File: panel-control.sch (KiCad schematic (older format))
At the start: 48 parts, among them J1 40HAT, J2 Conn_01x04, J3 103904-3, J4 HUB-75, J5 PWR, Q1 DMG2305UX, Q2 AO4407A, Q3 DMMT5401, SW1 RST, U1 STM8S003F3P, U2 TXS0108EPW, U3 TXS0108EPW

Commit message: fix labels and tweak pwr_en
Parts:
- removed J3: 103904-3, user_footprints:TE_103904-3, symbol 103904-3:103904-3
- added J4: HUB-75_B, user_footprints:TE_5-103167-5, symbol Connector_Generic:Conn_02x08_Odd_Even
- added J6: Conn_01x02_Male, symbol Connector:Conn_01x02_Male
- added R5: 5k, Resistor_SMD:R_0603_1608Metric, symbol Device:R
- added R7: 5k, symbol Device:R
- added U3: TXS0108EPW, Package_SO:TSSOP-20_4.4x6.5mm_P0.65mm, symbol Logic_LevelTranslator:TXS0108EPW
- C3: renamed from C6; value 1uF -> 100nF
- C4: renamed from C7; value 1uF -> 100nF
- J1: renamed from J5; footprint Connector_PinHeader_2.54mm:PinHeader_2x02_P2.54mm_Vertical -> Connector_PinHeader_2.54mm:PinHeader_2x04_P2.54mm_Vertical; symbol Connector_Generic:Conn_02x02_Odd_Even -> Connector_Generic:Conn_02x04_Odd_Even
- J3: renamed from J4; value HUB-75 -> HUB-75_A
- J5: renamed from J2; value Conn_01x04 -> SWIM
- MK1, MK2: symbol ICS-43434_DIP-6:ICS-43434 -> panel-control-rescue:ICS-43434-ICS-43434_DIP-6
- Q3: renamed from Q2; symbol AO4407A:AO4407A -> panel-control-rescue:AO4407A-AO4407A
- R6: renamed from R?; value 10k -> 1k
- gave numbers to parts that had none: 16
- renumbered C8 to C1, C2 to C10, C3 to C11, C4 to C12, C5 to C13, C9 to C2, C1 to C6, H3 to H2, H2 to H3, J1 to J2, Q3 to Q1, Q1 to Q2, R4 to R1, R1 to R2, R2 to R3, R3 to R4, SW1 to SW2, U3 to U1, U1 to U5
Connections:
- net labels added: B1A_A, B1A_B, B1B_A, B1B_B, B2A_A, B2A_B, B2B_A, B2B_B, G1A_A, G1A_B, G1B_A, G1B_B, G2A_A, G2A_B, G2B_A, G2B_B, I2S_OUT, R1A_A, R1A_B, R1B_A, R1B_B, R2A_A, R2A_B, R2B_A, R2B_B
- net labels removed: B1_A, B1_B, B2_A, B2_B, G1_A, G1_B, G2_A, G2_B, R1_A, R1_B, R2_A, R2_B, SCL_A, SCL_B, SDA_A, SDA_B, VBUS
- wire segments 199 -> 246
- no-connect marks 0 -> 3
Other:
- note added: "LED Panel Connectors"
- note removed: "LED Strip Connector"
- note removed: "SWIM"
- moved on the sheet: C10, C11, C12, C13, C6, J3, J5, R9, SW2

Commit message: mainly finished schematic revision
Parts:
- removed C6: 100nF, Capacitor_SMD:C_0603_1608Metric, symbol Device:C
- added C11: 100nF, Capacitor_SMD:C_0603_1608Metric, symbol Device:C
- added C12, C15: 100nF, Capacitor_SMD:C_0603_1608Metric_Pad1.08x0.95mm_HandSolder, symbol Device:C
- added D1: 5V, LED_SMD:LED_0603_1608Metric, symbol Device:LED
- added D3: PI, LED_SMD:LED_0603_1608Metric, symbol Device:LED
- added J6: POWER_CONN, symbol Connector:Conn_01x06_Male
- added R12: 4.7k, Resistor_SMD:R_0603_1608Metric, symbol Device:R
- added R14, R16: 470, Resistor_SMD:R_0603_1608Metric, symbol Device:R
- J2: renamed from J6; value Conn_01x02_Male -> VBAT
- R3: renamed from R5; value 5k -> 4.7k
- R5: renamed from R6; value 1k -> 4.7k
- R7: value 5k -> 10k
- SW1: value RST -> POW
- SW2: value RST -> NRST
- renumbered C7 to C1, C5 to C10, C1 to C13, C2 to C14, C9 to C2, C10 to C3, C11 to C4, C12 to C5, C13 to C6, C8 to C7, C3 to C8, C4 to C9, D1 to D2, D2 to D4, H3 to H2, H2 to H3, J2 to J1, J1 to J5, J5 to J7, Q3 to Q1, Q4 to Q2, Q2 to Q3, Q1 to Q4, R9 to R1, R4 to R10, R8 to R11, R1 to R13, R11 to R15, R12 to R17, R10 to R2, R13 to R4, R14 to R6, R3 to R8, R2 to R9, U4 to U1, U5 to U2, U2 to U3, U1 to U4, U3 to U5
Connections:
- net +3.3VA: now also C15.1
- net +3V3: now also J6.1 (Pin_1), R12.1
- net +5VA: now also Q1.1, Q1.2, Q1.3, R3.2, C12.1, R14.1; no longer Q3.3 (D), Q4.6 (E)
- net GND: now also C11.1, C12.2, C15.2, D1.1 (K), J6.6 (Pin_6); no longer D4.1 (K)
- net LED_BAT: now also J6.5 (Pin_5)
- net LED_PWR: now also J6.4 (Pin_4)
- net P5V_HAT: now also Q3.2 (S), Q4.6 (E), R16.1; no longer Q1.5, Q1.6, Q1.7, Q1.8
- net at Q3.1 (G), R8.1: now also Q4.1 (C); no longer Q4.4 (C)
- net NRST: now reaches SW2.1, U2.4 (NRST)
- net NRST: now also C11.2, J6.3 (Pin_3), R12.2; no longer J7.4 (Pin_4)
- net POW renamed BUT_POW
- new net: Q4.2 (B), Q4.3 (B), Q4.4 (C), R9.1
- new net: D3.1 (K), D4.1 (K)
- new net: D1.2 (A), R14.2
- new net: D3.2 (A), R16.2
- new net BUT_PWR: J6.2 (Pin_2)
- new net EXT_5V: Q1.5, Q1.6, Q1.7, Q1.8, Q3.3 (D), Q4.5 (E)
- new net RST: J7.4 (Pin_4)
- no-connect marks 3 -> 11
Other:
- note added: "I think this is intended to block excessive current\nfrom flowing from the Pi to the Hat, but actually idk.."
- note removed: "This is based on the official Raspberry Pi spec to be able to call an extension board a HAT.\nhttps://github.com/raspberrypi/hats/blob/master/designguide.md"
- moved on the sheet: C1, C10, C13, C14, C2, C3, C4, C5, C6, C7, D2, D4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

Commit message: update pcb from new sch
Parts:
- C3, C4, C5, C6: footprint (none) -> Capacitor_SMD:C_0603_1608Metric
- C7, R7: footprint (none) -> Resistor_SMD:R_0603_1608Metric
- J2: footprint (none) -> Connector_PinHeader_2.54mm:PinHeader_1x02_P2.54mm_Vertical
- J6: footprint (none) -> Connector_PinHeader_2.54mm:PinHeader_1x06_P2.54mm_Vertical
- J7: footprint (none) -> Connector_PinHeader_2.54mm:PinHeader_1x04_P2.54mm_Vertical
- Q2: footprint Package_TO_SOT_THT:TO-92_Inline -> Package_TO_SOT_SMD:SOT-23
- U1: value AMS1117-3.3 -> HT7533-1; footprint Package_TO_SOT_SMD:SOT-223-3_TabPin2 -> Package_TO_SOT_SMD:SOT-89-3; symbol Regulator_Linear:AMS1117-3.3 -> Regulator_Linear:HT75xx-1-SOT89; LCSC C6186 -> C14289
- U2: value STM8S003F3P -> STM8S103F3P
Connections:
- net +3V3: now also U1.3 (VOUT); no longer U1.2 (VO)
- net +5VA: now also U1.2 (VIN); no longer U1.3 (VI)
- no-connect marks 11 -> 19
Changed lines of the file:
@@
 P 13000 3300
 F 0 "U2" H 13000 4481 50  0000 C CNN
-F 1 "STM8S003F3P" H 13000 4390 50  0000 C CNN
+F 1 "STM8S103F3P" H 13000 4390 50  0000 C CNN
 F 2 "Package_SO:TSSOP-20_4.4x6.5mm_P0.65mm" H 13050 4400 50  0001 L CNN
 F 3 "http://www.st.com/st-web-ui/static/active/en/resource/technical/document/datasheet/DM00024550.pdf" H 12950 2900 50  0001 C CNN
@@
 F 0 "J7" H 1068 9967 50  0000 C CNN
 F 1 "SWIM" H 1068 9876 50  0000 C CNN
-F 2 "" H 1150 9650 50  0001 C CNN
+F 2 "Connector_PinHeader_2.54mm:PinHeader_1x04_P2.54mm_Vertical" H 1150 9650 50  0001 C CNN
 F 3 "~" H 1150 9650 50  0001 C CNN
 	1    1150 9650
@@
 F 0 "C3" H 13486 1604 50  0000 R CNN
 F 1 "100nF" H 13486 1695 50  0000 R CNN
-F 2 "" H 13638 1500 50  0001 C CNN
+F 2 "Capacitor_SMD:C_0603_1608Metric" H 13638 1500 50  0001 C CNN
 F 3 "~" H 13600 1650 50  0001 C CNN
 	1    13600 1650
@@
 F 0 "C4" H 13736 1604 50  0000 R CNN
 F 1 "100nF" H 13736 1695 50  0000 R CNN
-F 2 "" H 13888 1500 50  0001 C CNN
+F 2 "Capacitor_SMD:C_0603_1608Metric" H 13888 1500 50  0001 C CNN
 F 3 "~" H 13850 1650 50  0001 C CNN
 	1    13850 1650
@@
 F 0 "C7" H 12085 4104 50  0000 R CNN
 F 1 "1uF" H 12085 4195 50  0000 R CNN
-F 2 "" H 12238 4000 50  0001 C CNN
+F 2 "Resistor_SMD:R_0603_1608Metric" H 12238 4000 50  0001 C CNN
 F 3 "~" H 12200 4150 50  0001 C CNN
 	1    12200 4150
@@
 F 3 "" H 14450 3400 50  0000 C CNN
 	1    14450 3400
-	1    0    0    -1
-$EndComp
-$Comp
-L Regulator_Linear:AMS1117-3.3 U1
-U 1 1 601B9BE5
-P 12500 1500
-F 0 "U1" H 12500 1742 50  0000 C CNN
-F 1 "AMS1117-3.3" H 12500 1651 50  0000 C CNN
-F 2 "Package_TO_SOT_SMD:SOT-223-3_TabPin2" H 12500 1700 50  0001 C CNN
-F 3 "http://www.advanced-monolithic.com/pdf/ds1117.pdf" H 12600 1250 50  0001 C CNN
-F 4 "C6186" H 12500 1500 50  0001 C CNN "LCSC"
-	1    12500 1500
 	1    0    0    -1
 $EndComp
@@
 F 0 "Q2" H 9341 2096 50  0000 L CNN
 F 1 "S8050" H 9341 2005 50  0000 L CNN
-F 2 "Package_TO_SOT_THT:TO-92_Inline" H 9350 1975 50  0001 L CIN
+F 2 "Package_TO_SOT_SMD:SOT-23" H 9350 1975 50  0001 L CIN
 F 3 "http://www.unisonic.com.tw/datasheet/S8050.pdf" H 9150 2050 50  0001 L CNN
 	1    9150 2050
@@
 F 0 "J2" H 15072 3024 50  0000 R CNN
 F 1 "VBAT" H 15072 2933 50  0000 R CNN
-F 2 "" H 15100 3050 50  0001 C CNN
+F 2 "Connector_PinHeader_2.54mm:PinHeader_1x02_P2.54mm_Vertical" H 15100 3050 50  0001 C CNN
 F 3 "~" H 15100 3050 50  0001 C CNN
 	1    15100 3050
@@
 F 0 "R7" H 9770 2246 50  0000 L CNN
 F 1 "10k" H 9770 2155 50  0000 L CNN
-F 2 "" V 9630 2200 50  0001 C CNN
+F 2 "Resistor_SMD:R_0603_1608Metric" V 9630 2200 50  0001 C CNN
 F 3 "~" H 9700 2200 50  0001 C CNN
 	1    9700 2200
@@
 F 0 "C6" H 14236 1604 50  0000 R CNN
 F 1 "100nF" H 14236 1695 50  0000 R CNN
-F 2 "" H 14388 1500 50  0001 C CNN
+F 2 "Capacitor_SMD:C_0603_1608Metric" H 14388 1500 50  0001 C CNN
 F 3 "~" H 14350 1650 50  0001 C CNN
 	1    14350 1650
@@
 F 0 "C5" H 13986 1604 50  0000 R CNN
 F 1 "100nF" H 13986 1695 50  0000 R CNN
-F 2 "" H 14138 1500 50  0001 C CNN
+F 2 "Capacitor_SMD:C_0603_1608Metric" H 14138 1500 50  0001 C CNN
 F 3 "~" H 14100 1650 50  0001 C CNN
 	1    14100 1650
@@
 F 0 "J6" H 1258 8431 50  0000 C CNN
 F 1 "POWER_CONN" H 1258 8340 50  0000 C CNN
-F 2 "" H 1150 8050 50  0001 C CNN
+F 2 "Connector_PinHeader_2.54mm:PinHeader_1x06_P2.54mm_Vertical" H 1150 8050 50  0001 C CNN
 F 3 "~" H 1150 8050 50  0001 C CNN
 	1    1150 8050
@@
 Text Label 7650 2150 0    50   ~ 0
 EXT_5V
+NoConn ~ 12400 3400
+NoConn ~ 12400 2800
+NoConn ~ 12400 2700
+NoConn ~ 12400 3500
+NoConn ~ 12400 3600
+NoConn ~ 12400 3700
+NoConn ~ 13600 3200
+NoConn ~ 13600 3300
+$Comp
+L Regulator_Linear:HT75xx-1-SOT89 U1
+U 1 1 601B9BE5
+P 12500 1600
+F 0 "U1" H 12500 1842 50  0000 C CNN
+F 1 "HT7533-1" H 12500 1751 50  0000 C CNN
+F 2 "Package_TO_SOT_SMD:SOT-89-3" H 12500 1800 50  0001 C CNN
+F 3 "https://www.holtek.com/documents/10179/116711/HT75xx-1v250.pdf" H 12600 1350 50  0001 C CNN
+F 4 "C14289" H 12500 1600 50  0001 C CNN "LCSC"
+	1    12500 1600
+	1    0    0    -1
+$EndComp
 $EndSCHEMATC

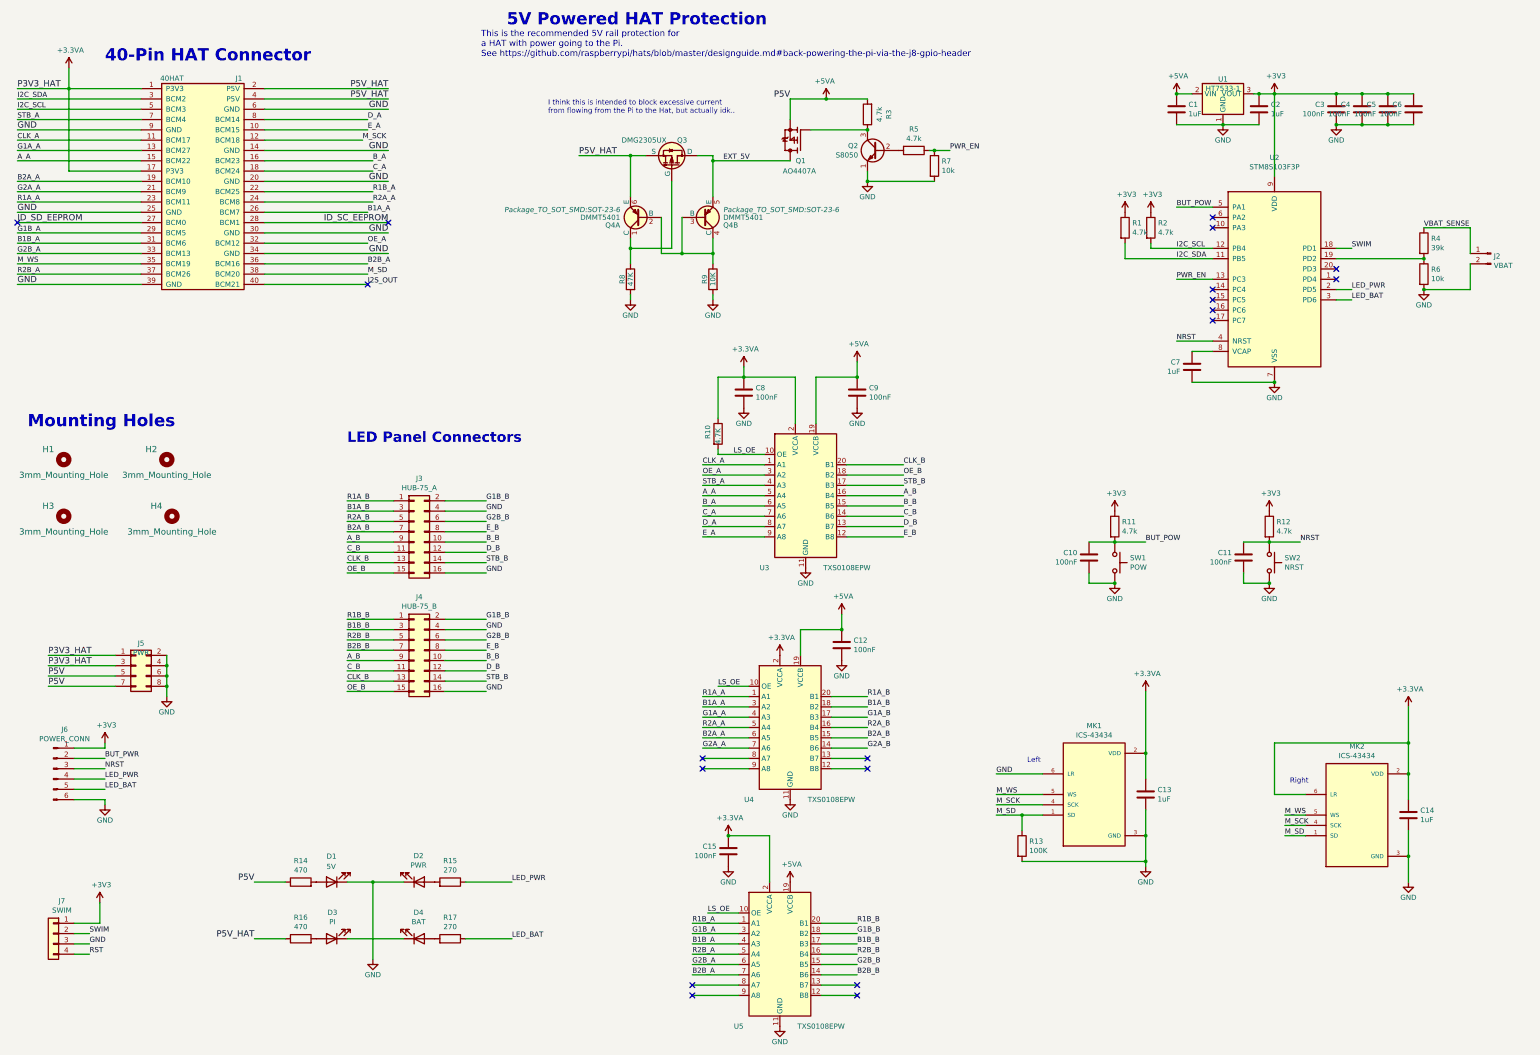
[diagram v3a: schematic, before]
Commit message: add fan connector to sch
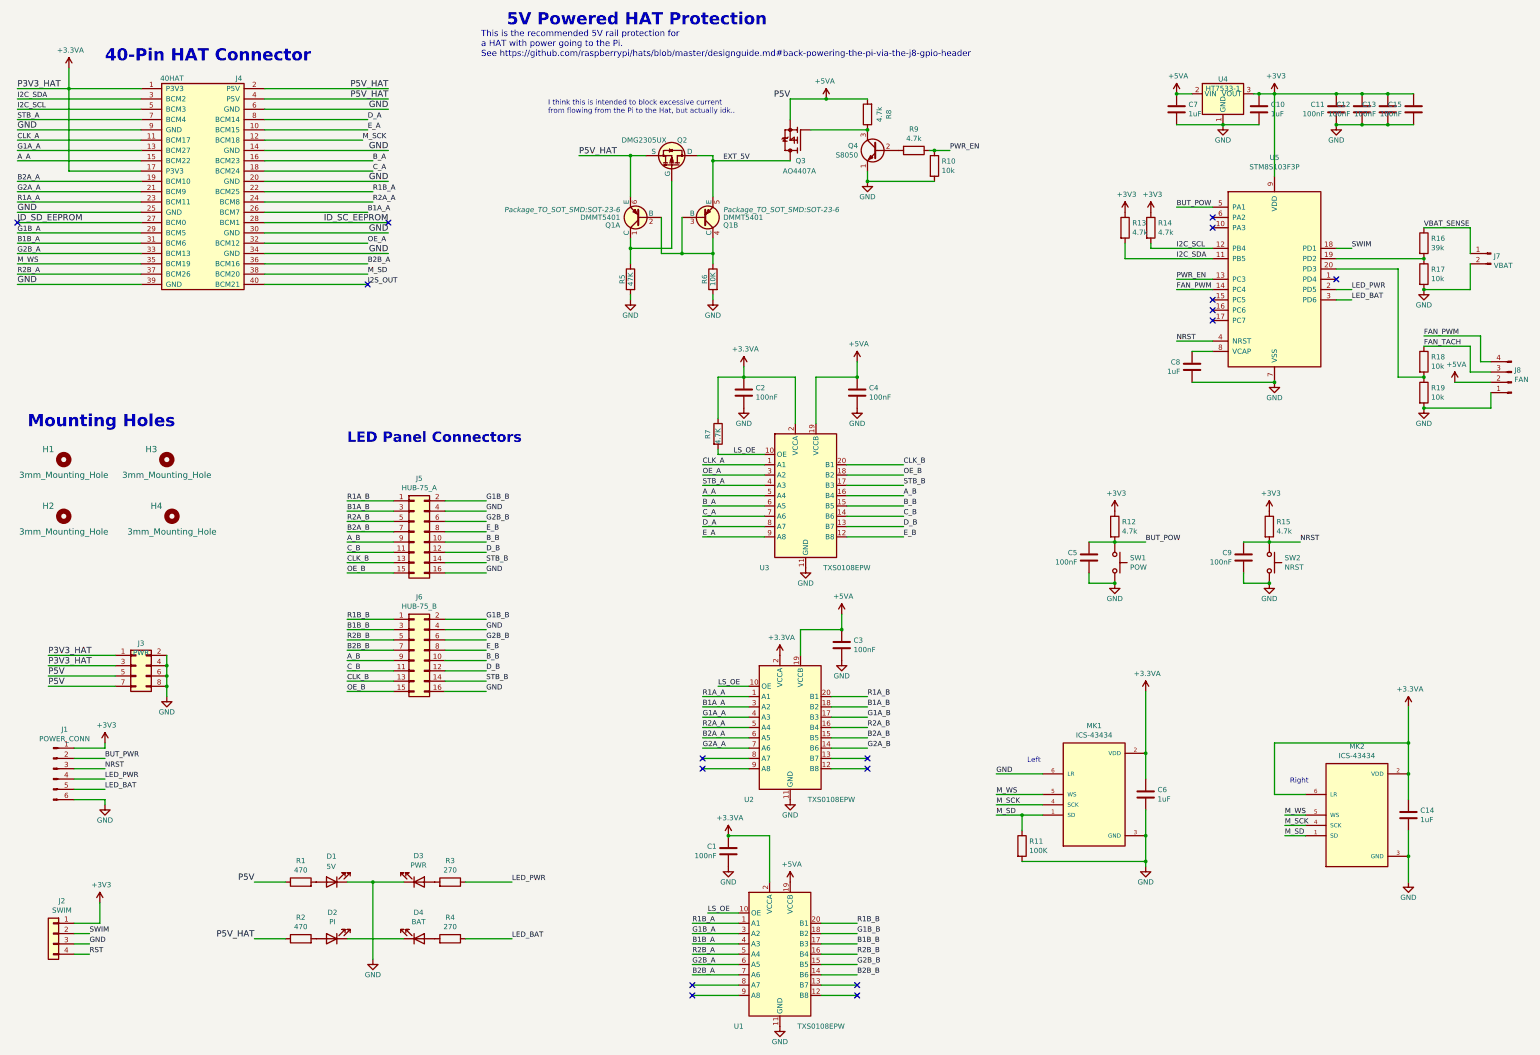
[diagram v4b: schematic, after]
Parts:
- added J8: FAN, Connector_PinSocket_2.54mm:PinSocket_1x04_P2.54mm_Vertical, symbol Connector:Conn_01x04_Male
- added R18, R19: 10k, Resistor_SMD:R_0603_1608Metric, symbol Device:R
- renumbered C15 to C1, C2 to C10, C3 to C11, C4 to C12, C5 to C13, C6 to C15, C8 to C2, C12 to C3, C9 to C4, C10 to C5, C13 to C6, C1 to C7, C7 to C8, C11 to C9, D3 to D2, D2 to D3, H3 to H2, H2 to H3, J6 to J1, J7 to J2, J5 to J3, J1 to J4, J3 to J5, J4 to J6, J2 to J7, Q4 to Q1, Q3 to Q2, Q1 to Q3, Q2 to Q4, R14 to R1, R7 to R10, R13 to R11, R11 to R12, R1 to R13, R2 to R14, R12 to R15, R4 to R16, R6 to R17, R16 to R2, R15 to R3, R17 to R4, R8 to R5, R9 to R6, R10 to R7, R3 to R8, R5 to R9, U5 to U1, U4 to U2, U1 to U4, U2 to U5
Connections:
- net +5VA: now also J8.2 (Pin_2)
- net GND: now also J8.1 (Pin_1), R19.2
- net FAN_PWM: now reaches U5.14 (PC4)
- net FAN_PWM: now also J8.4 (Pin_4)
- net at U5.20 (PD3): now also R18.2, R19.1
- new net FAN_TACH: J8.3 (Pin_3), R18.1
- no-connect marks 19 -> 17

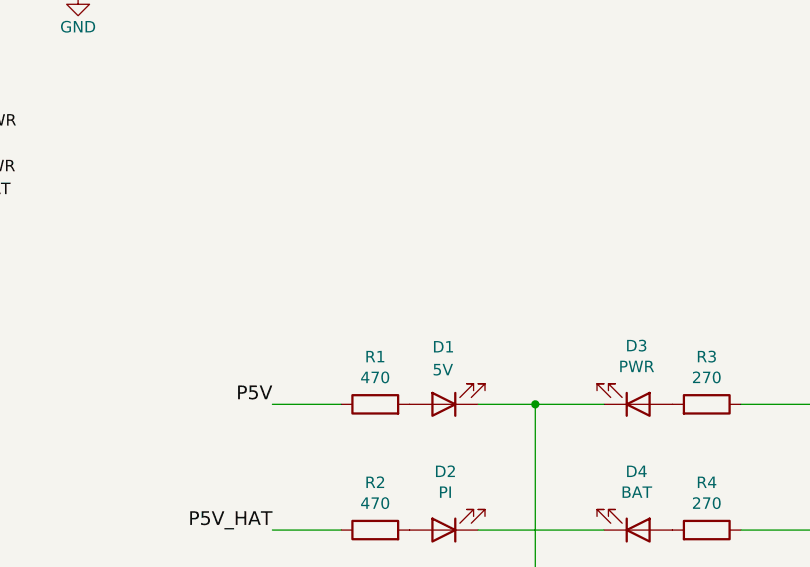
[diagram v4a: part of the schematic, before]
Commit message: fix footprints
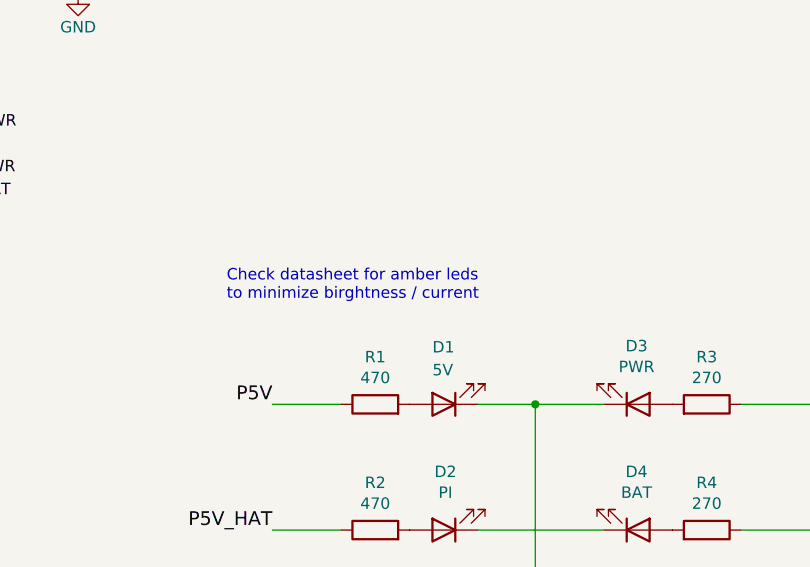
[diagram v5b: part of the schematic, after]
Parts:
- J5, J6: footprint user_footprints:TE_5-103167-5 -> Connector_IDC:IDC-Header_2x08_P2.54mm_Vertical
- J8: footprint Connector_PinSocket_2.54mm:PinSocket_1x04_P2.54mm_Vertical -> Connector:FanPinHeader_1x04_P2.54mm_Vertical
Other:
- note added: "Check datasheet for amber leds \nto minimize birghtness / current"
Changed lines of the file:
@@
 F 0 "J5" H 4700 6267 50  0000 C CNN
 F 1 "HUB-75_A" H 4700 6176 50  0000 C CNN
-F 2 "user_footprints:TE_5-103167-5" H 4650 5750 50  0001 C CNN
+F 2 "Connector_IDC:IDC-Header_2x08_P2.54mm_Vertical" H 4650 5750 50  0001 C CNN
 F 3 "~" H 4650 5750 50  0001 C CNN
 	1    4650 5750
@@
 F 0 "J6" H 4700 7417 50  0000 C CNN
 F 1 "HUB-75_B" H 4700 7326 50  0000 C CNN
-F 2 "user_footprints:TE_5-103167-5" H 4650 6900 50  0001 C CNN
+F 2 "Connector_IDC:IDC-Header_2x08_P2.54mm_Vertical" H 4650 6900 50  0001 C CNN
 F 3 "~" H 4650 6900 50  0001 C CNN
 	1    4650 6900
@@
 F 0 "J8" H 15272 4182 50  0000 R CNN
 F 1 "FAN" H 15272 4273 50  0000 R CNN
-F 2 "Connector_PinSocket_2.54mm:PinSocket_1x04_P2.54mm_Vertical" H 15300 4300 50  0001 C CNN
+F 2 "Connector:FanPinHeader_1x04_P2.54mm_Vertical" H 15300 4300 50  0001 C CNN
 F 3 "~" H 15300 4300 50  0001 C CNN
 	1    15300 4300
@@
 Wire Wire Line
 	15000 4100 15100 4100
+Text Notes 2900 8700 0    50   ~ 0
+Check datasheet for amber leds \nto minimize birghtness / current
 $EndSCHEMATC

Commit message: work on new pcb layout
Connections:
- net EXT_5V: no longer Q3.5, Q3.6, Q3.7, Q3.8
- net GND: now also D2.1 (K), D4.1 (K)
- net P5V_HAT: now also Q3.5, Q3.6, Q3.7, Q3.8; no longer Q1.6 (E), Q2.2 (S)
- new net: Q1.6 (E), Q2.2 (S)
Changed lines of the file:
@@
 	1    0    0    -1
 $EndComp
-Text Label 6250 2100 0    60   ~ 0
+Text Label 7800 2150 0    60   ~ 0
 P5V_HAT
 Wire Wire Line
@@
 	7050 3050 7050 2700
 Connection ~ 7250 3050
-Wire Wire Line
-	7550 2500 7550 2150
 Wire Wire Line
 	6750 2500 6750 2100
@@
 Wire Wire Line
 	8650 1550 9050 1550
-Wire Wire Line
-	8300 2150 7550 2150
-Connection ~ 7550 2150
-Wire Wire Line
-	7550 2150 7550 2100
 Text Notes 5950 1700 0    50   ~ 0
 I think this is intended to block excessive current\nfrom flowing from the Pi to the Hat, but actually idk..
@@
 	4550 9150 4250 9150
 Wire Wire Line
-	4550 9700 4000 9700
+	4550 9700 4250 9700
 $Comp
 L power:GND #PWR06
@@
 	-1   0    0    -1
 $EndComp
-Wire Wire Line
-	4250 9900 4250 9150
 Connection ~ 4250 9150
 Wire Wire Line
@@
 Wire Wire Line
 	1650 8350 1650 8400
-Text Label 7650 2150 0    50   ~ 0
+Text Label 7400 2100 0    50   ~ 0
 EXT_5V
 NoConn ~ 12400 2800
@@
 Text Notes 2900 8700 0    50   ~ 0
 Check datasheet for amber leds \nto minimize birghtness / current
+Wire Wire Line
+	7550 2100 7550 2500
+Wire Wire Line
+	7800 2150 8300 2150
+Wire Wire Line
+	4250 9150 4250 9700
+Connection ~ 4250 9700
+Wire Wire Line
+	4250 9700 4000 9700
+Wire Wire Line
+	4250 9700 4250 9900
 $EndSCHEMATC
